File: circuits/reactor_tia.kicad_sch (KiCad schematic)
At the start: 18 parts, among them J1 Conn_01x04, J2 Conn_01x02, U1 OPA380AID, U2 OPA380AID

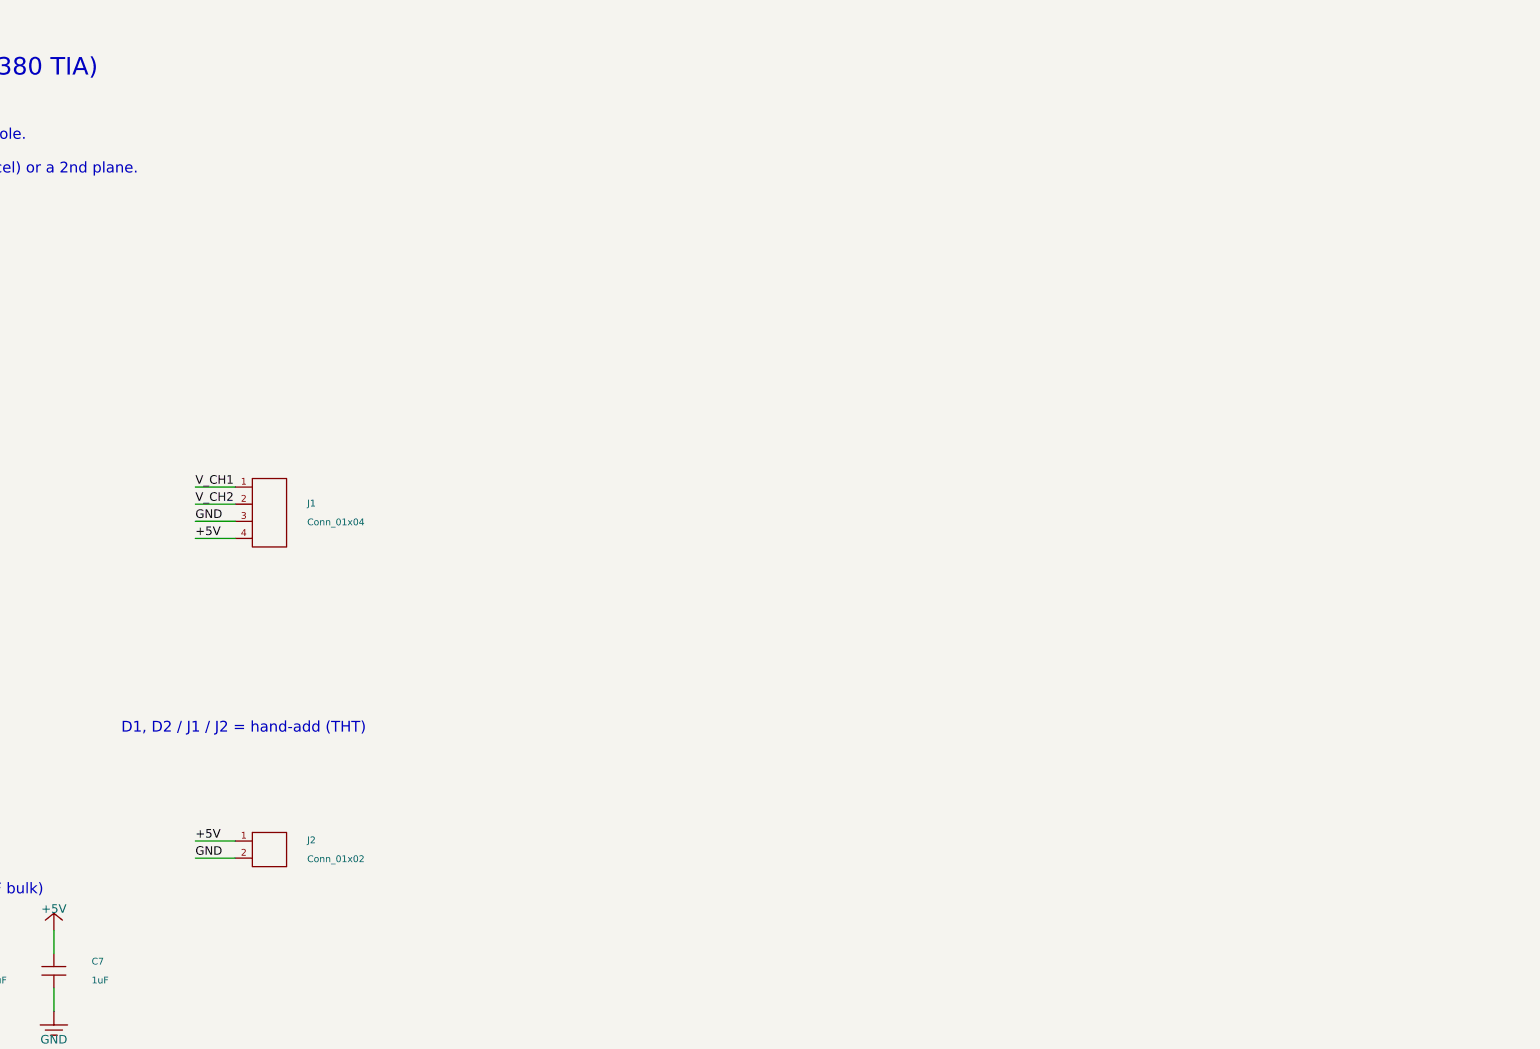
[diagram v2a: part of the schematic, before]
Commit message: feat(bench): add reactor optics control updates
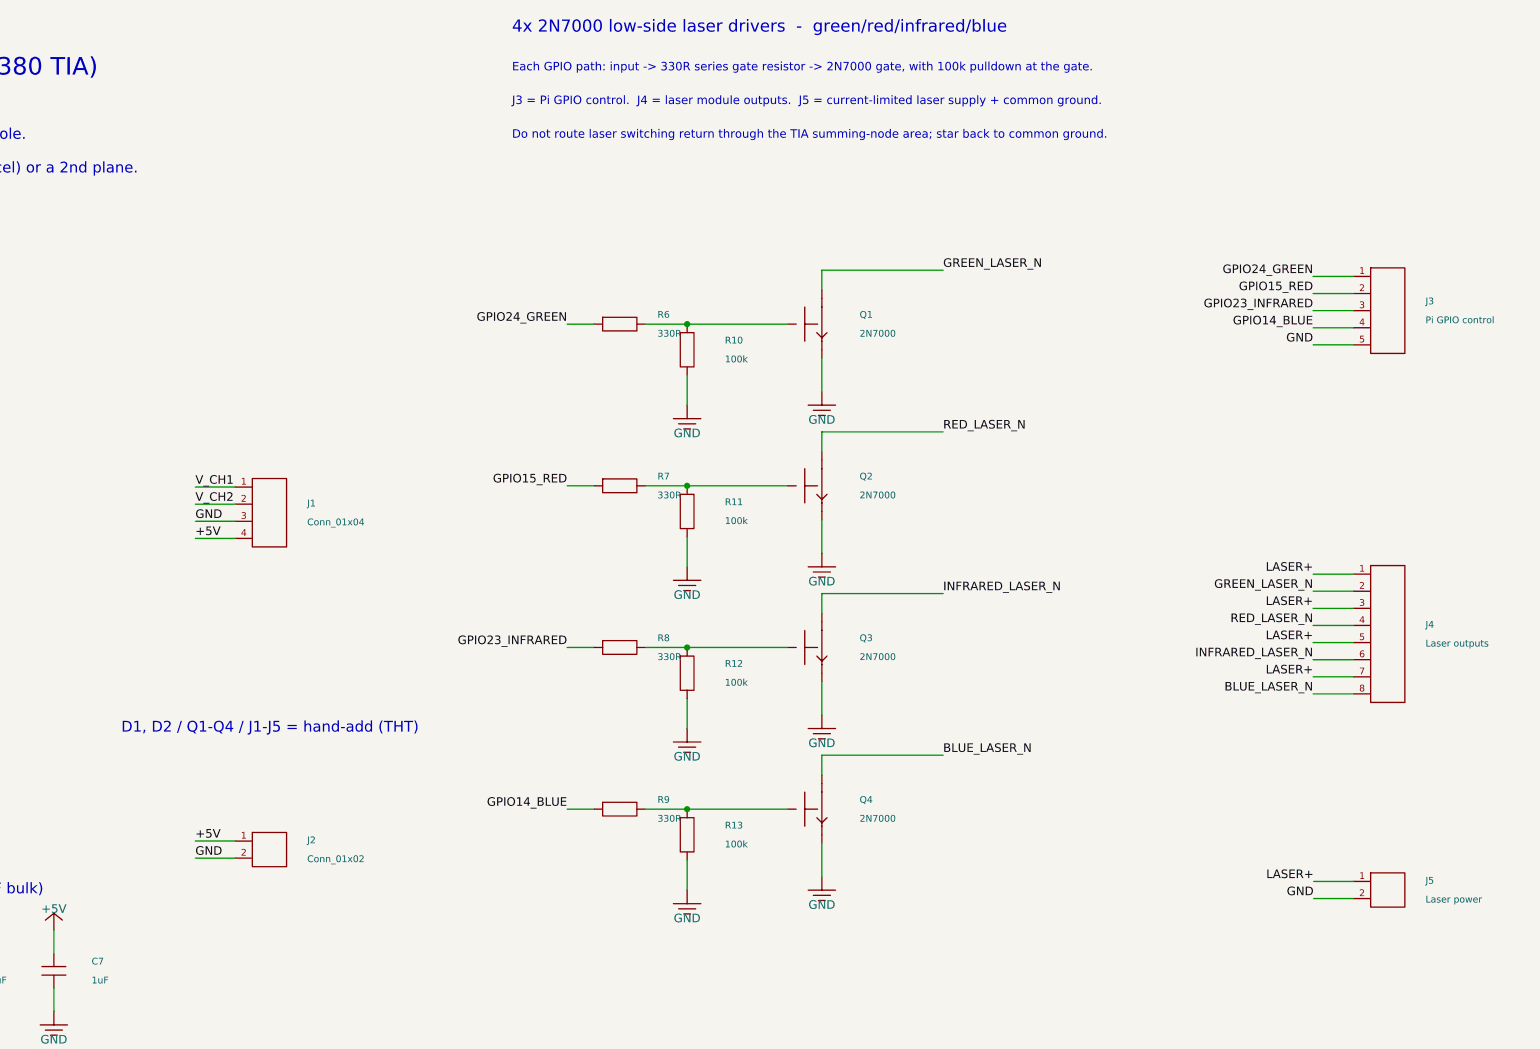
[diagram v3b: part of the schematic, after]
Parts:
- added J3: Pi GPIO control, Connector_PinHeader_2.54mm:PinHeader_1x05_P2.54mm_Vertical, symbol viv:CONN5
- added J4: Laser outputs, Connector_PinHeader_2.54mm:PinHeader_1x08_P2.54mm_Vertical, symbol viv:CONN8
- added J5: Laser power, Connector_PinHeader_2.54mm:PinHeader_1x02_P2.54mm_Vertical, symbol viv:CONN2
- added Q1, Q2, Q3, Q4: 2N7000, Package_TO_SOT_THT:TO-92_Inline, symbol viv:MOS_N
- added R10, R11, R12, R13: 100k, Resistor_SMD:R_0603_1608Metric_Pad0.98x0.95mm_HandSolder, symbol viv:R_V
- added R6, R7, R8, R9: 330R, Resistor_SMD:R_0603_1608Metric_Pad0.98x0.95mm_HandSolder, symbol viv:R_H
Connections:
- net GND: now also J3.5, J5.2, Q1.1 (S), Q2.1 (S), Q3.1 (S), Q4.1 (S), R10.2, R11.2, R12.2, R13.2
- new net: Q1.2 (G), R10.1, R6.2
- new net: Q2.2 (G), R11.1, R7.2
- new net: Q3.2 (G), R12.1, R8.2
- new net: Q4.2 (G), R13.1, R9.2
- new net BLUE_LASER_N: J4.8, Q4.3 (D)
- new net GPIO14_BLUE: J3.4, R9.1
- new net GPIO15_RED: J3.2, R7.1
- new net GPIO23_INFRARED: J3.3, R8.1
- new net GPIO24_GREEN: J3.1, R6.1
- new net GREEN_LASER_N: J4.2, Q1.3 (D)
- new net INFRARED_LASER_N: J4.6, Q3.3 (D)
- new net LASER+: J4.1, J4.3, J4.5, J4.7, J5.1
- new net RED_LASER_N: J4.4, Q2.3 (D)
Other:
- note added: "4x 2N7000 low-side laser drivers - green/red/infrared/blue"
- note added: "D1, D2 / Q1-Q4 / J1-J5 = hand-add (THT)"
- note added: "Do not route laser switching return through the TIA summing-node area; star back to common ground."
- note added: "Each GPIO path: input -> 330R series gate resistor -> 2N7000 gate, with 100k pulldown at the gate."
- note added: "J3 = Pi GPIO control. J4 = laser module outputs. J5 = current-limited laser supply + common ground."
- note removed: "D1, D2 / J1 / J2 = hand-add (THT)"
- title: Reactor TIA - 2 channels x 1 OPA380AID -> Reactor TIA + 4-channel 2N7000 laser driver
